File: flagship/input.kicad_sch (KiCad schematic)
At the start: 24 parts, among them Q1 PSMN3R7-100BSE, Q2 PSMN3R7-100BSE, U1 LTC4364IS-1

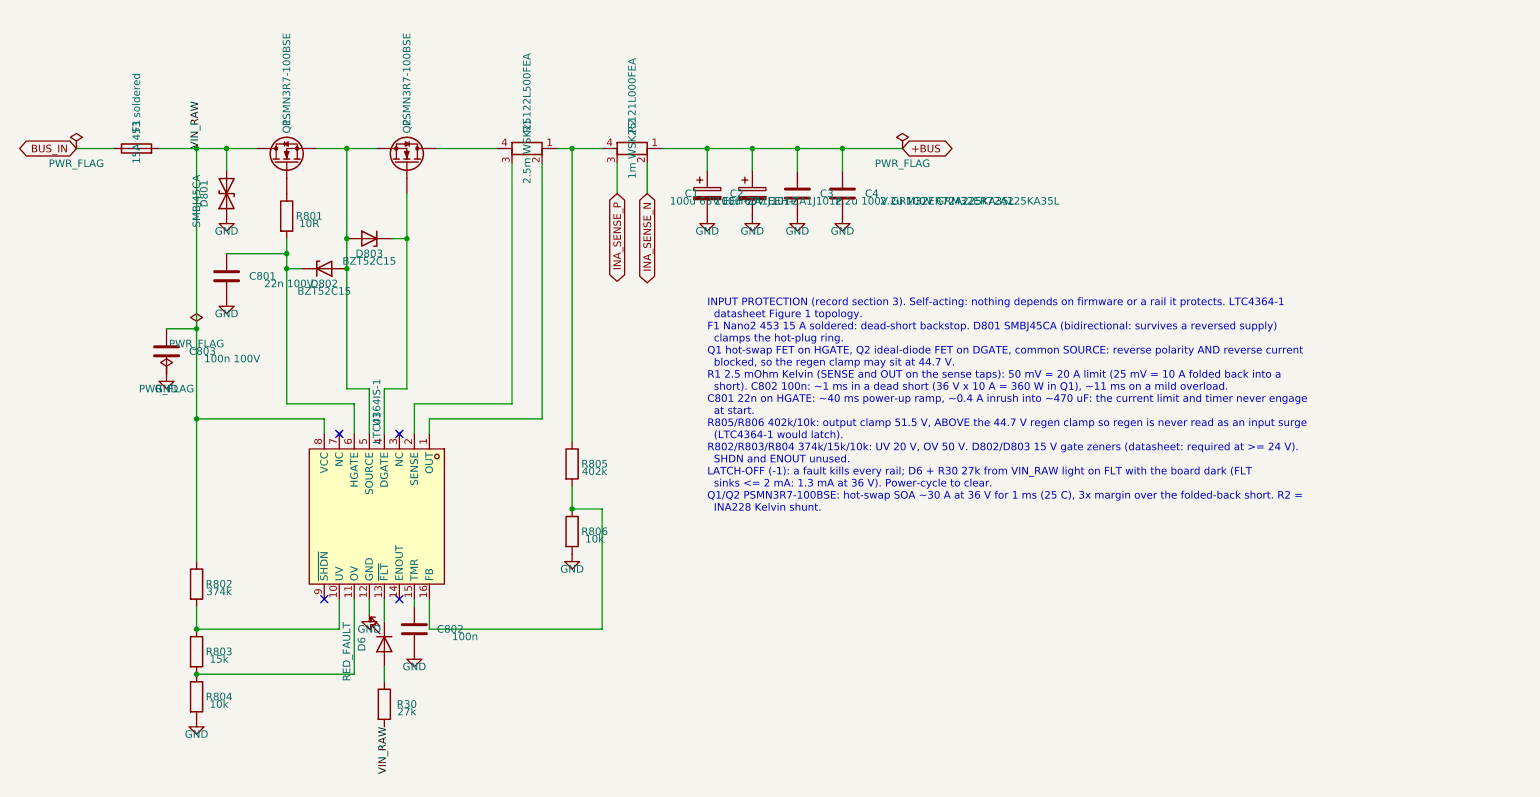
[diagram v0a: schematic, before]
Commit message: flagship: shunts to LCSC stock -- WSK1216 true Kelvin for the INA228, CSS2H 2 mOhm pseudo-Kelvin (net-tied sense pads) for the LTC4364 and motor switch
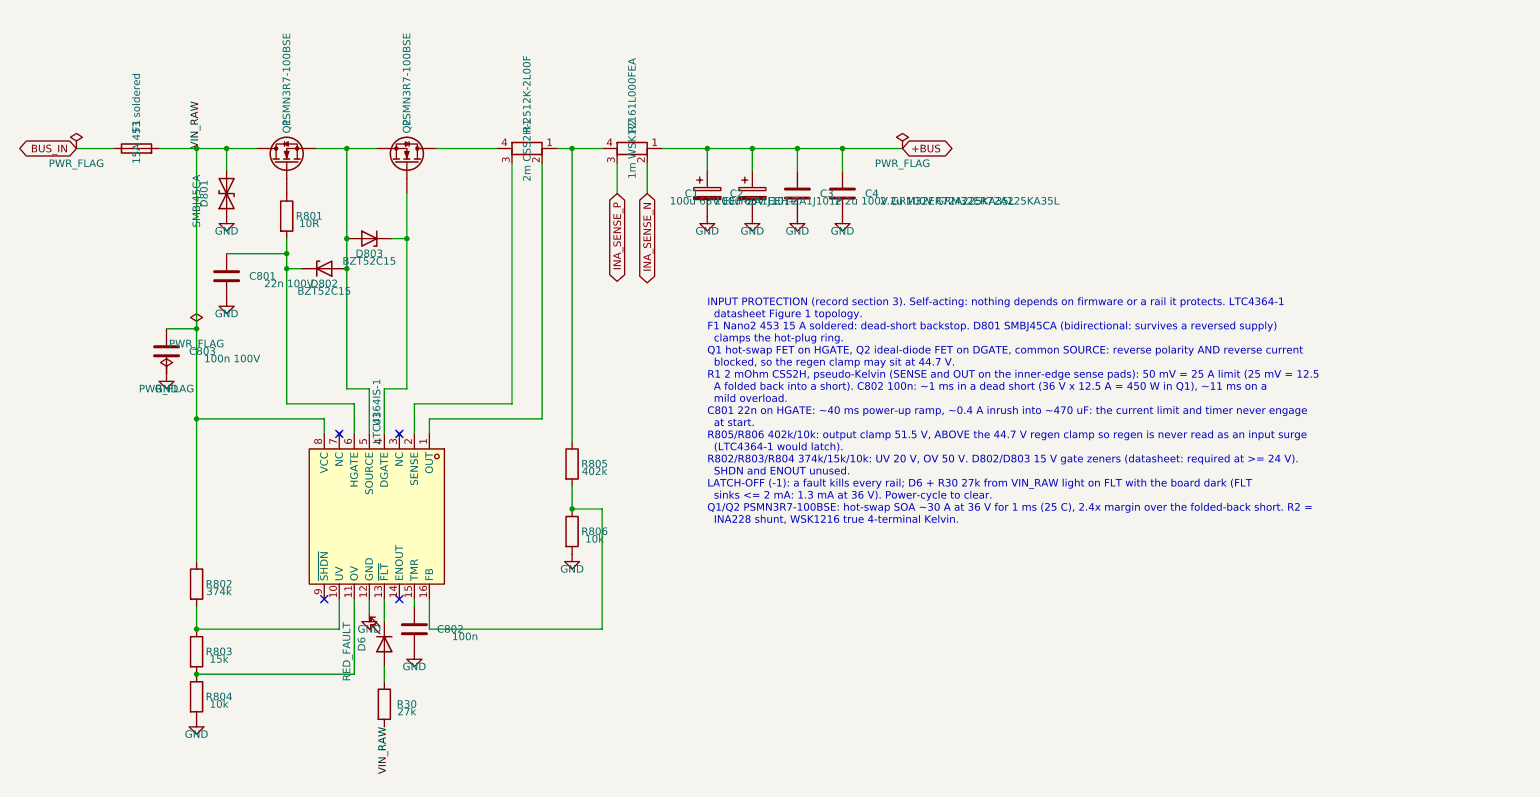
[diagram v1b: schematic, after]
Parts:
- R1: value 2.5m WSK25122L500FEA -> 2m CSS2H-2512K-2L00F; footprint Resistor_SMD:R_Shunt_Vishay_WSK2512_6332Metric_T2.21mm -> flagship:R_2512_Shunt_PseudoKelvin
- R2: value 1m WSK25121L000FEA -> 1m WSK12161L000FEA; footprint Resistor_SMD:R_Shunt_Vishay_WSK2512_6332Metric_T2.21mm -> flagship:R_Shunt_Vishay_WSK1216_Kelvin
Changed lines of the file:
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@@
 	(generator_version "10.0")
 	(paper "A3")
-	(text "INPUT PROTECTION (record section 3). Self-acting: nothing depends on firmware or a rail it protects. LTC4364-1\n  datasheet Figure 1 topology.\nF1 Nano2 453 15 A soldered: dead-short backstop. D801 SMBJ45CA (bidirectional: survives a reversed supply)\n  clamps the hot-plug ring.\nQ1 hot-swap FET on HGATE, Q2 ideal-diode FET on DGATE, common SOURCE: reverse polarity AND reverse current\n  blocked, so the regen clamp may sit at 44.7 V.\nR1 2.5 mOhm Kelvin (SENSE and OUT on the sense taps): 50 mV = 20 A limit (25 mV = 10 A folded back into a\n  short). C802 100n: ~1 ms in a dead short (36 V x 10 A = 360 W in Q1), ~11 ms on a mild overload.\nC801 22n on HGATE: ~40 ms power-up ramp, ~0.4 A inrush into ~470 uF: the current limit and timer never engage\n  at start.\nR805/R806 402k/10k: output clamp 51.5 V, ABOVE the 44.7 V regen clamp so regen is never read as an input surge\n  (LTC4364-1 would latch).\nR802/R803/R804 374k/15k/10k: UV 20 V, OV 50 V. D802/D803 15 V gate zeners (datasheet: required at >= 24 V).\n  SHDN and ENOUT unused.\nLATCH-OFF (-1): a fault kills every rail; D6 + R30 27k from VIN_RAW light on FLT with the board dark (FLT\n  sinks <= 2 mA: 1.3 mA at 36 V). Power-cycle to clear.\nQ1/Q2 PSMN3R7-100BSE: hot-swap SOA ~30 A at 36 V for 1 ms (25 C), 3x margin over the folded-back short. R2 =\n  INA228 Kelvin shunt."
+	(text "INPUT PROTECTION (record section 3). Self-acting: nothing depends on firmware or a rail it protects. LTC4364-1\n  datasheet Figure 1 topology.\nF1 Nano2 453 15 A soldered: dead-short backstop. D801 SMBJ45CA (bidirectional: survives a reversed supply)\n  clamps the hot-plug ring.\nQ1 hot-swap FET on HGATE, Q2 ideal-diode FET on DGATE, common SOURCE: reverse polarity AND reverse current\n  blocked, so the regen clamp may sit at 44.7 V.\nR1 2 mOhm CSS2H, pseudo-Kelvin (SENSE and OUT on the inner-edge sense pads): 50 mV = 25 A limit (25 mV = 12.5\n  A folded back into a short). C802 100n: ~1 ms in a dead short (36 V x 12.5 A = 450 W in Q1), ~11 ms on a\n  mild overload.\nC801 22n on HGATE: ~40 ms power-up ramp, ~0.4 A inrush into ~470 uF: the current limit and timer never engage\n  at start.\nR805/R806 402k/10k: output clamp 51.5 V, ABOVE the 44.7 V regen clamp so regen is never read as an input surge\n  (LTC4364-1 would latch).\nR802/R803/R804 374k/15k/10k: UV 20 V, OV 50 V. D802/D803 15 V gate zeners (datasheet: required at >= 24 V).\n  SHDN and ENOUT unused.\nLATCH-OFF (-1): a fault kills every rail; D6 + R30 27k from VIN_RAW light on FLT with the board dark (FLT\n  sinks <= 2 mA: 1.3 mA at 36 V). Power-cycle to clear.\nQ1/Q2 PSMN3R7-100BSE: hot-swap SOA ~30 A at 36 V for 1 ms (25 C), 2.4x margin over the folded-back short. R2 =\n  INA228 shunt, WSK1216 true 4-terminal Kelvin."
 		(exclude_from_sim no)
 		(at 127 76.2 0)
@@
 			)
 		)
-		(property "Value" "2.5m WSK25122L500FEA"
+		(property "Value" "2m CSS2H-2512K-2L00F"
 			(at 96.52 45.72 0)
 			(show_name no)
@@
 			)
 		)
-		(property "Footprint" "Resistor_SMD:R_Shunt_Vishay_WSK2512_6332Metric_T2.21mm"
+		(property "Footprint" "flagship:R_2512_Shunt_PseudoKelvin"
 			(at 94.74 50.8 90)
 			(hide yes)
@@
 			)
 		)
-		(property "Value" "1m WSK25121L000FEA"
+		(property "Value" "1m WSK12161L000FEA"
 			(at 114.3 45.72 0)
 			(show_name no)
@@
 			)
 		)
-		(property "Footprint" "Resistor_SMD:R_Shunt_Vishay_WSK2512_6332Metric_T2.21mm"
+		(property "Footprint" "flagship:R_Shunt_Vishay_WSK1216_Kelvin"
 			(at 112.52 50.8 90)
 			(hide yes)

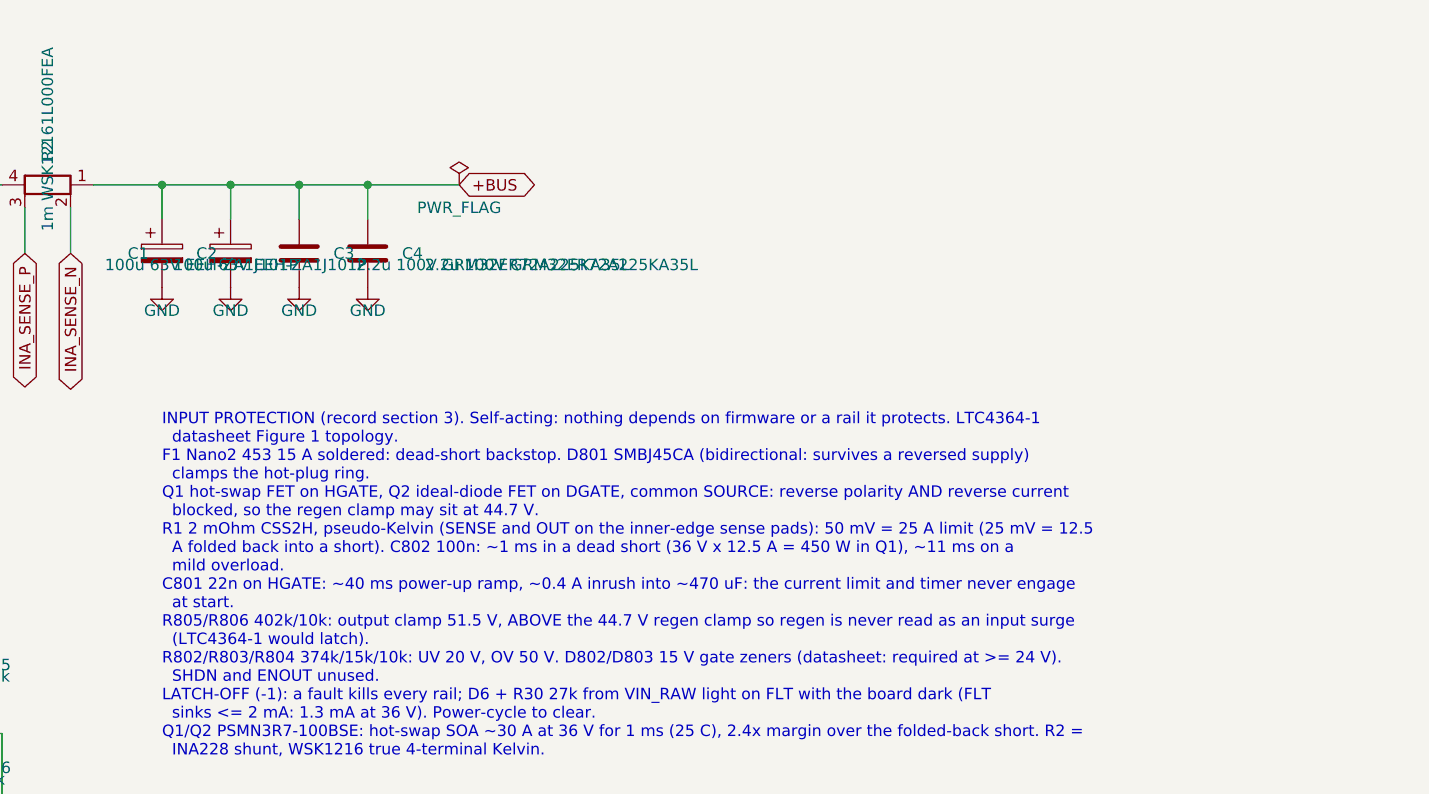
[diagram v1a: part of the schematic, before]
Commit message: flagship: bulk to 4 x EEH-ZA1J101P (C5/C6 on +BUS); input note tracks the 44.5 V clamp and the ~670 uF inrush
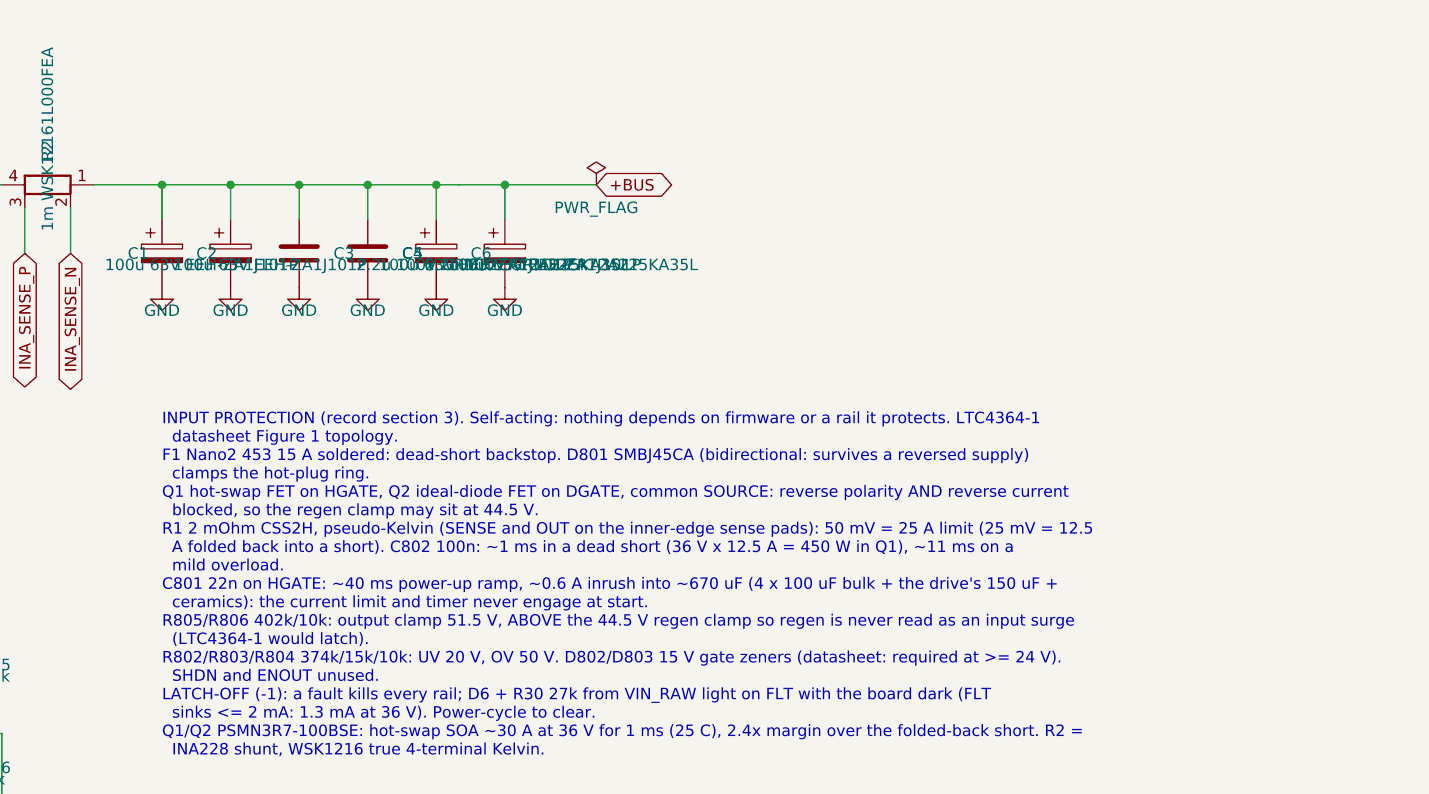
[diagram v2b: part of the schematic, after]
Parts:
- added C5, C6: 100u 63V EEH-ZA1J101P, Capacitor_SMD:CP_Elec_10x10.5, symbol Device:C_Polarized
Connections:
- net +BUS: now also C5.1, C6.1
- net GND: now also C5.2, C6.2
